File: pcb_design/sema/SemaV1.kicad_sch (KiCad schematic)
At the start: 22 parts, among them IC1 PIC24FJ64GA002-I_SP, J1 Conn_01x05_Pin, J2 Conn_01x02_Pin, J3 Conn_01x02_Pin, J4 Conn_01x04_Pin, U1 ESP8266-01_ESP-01

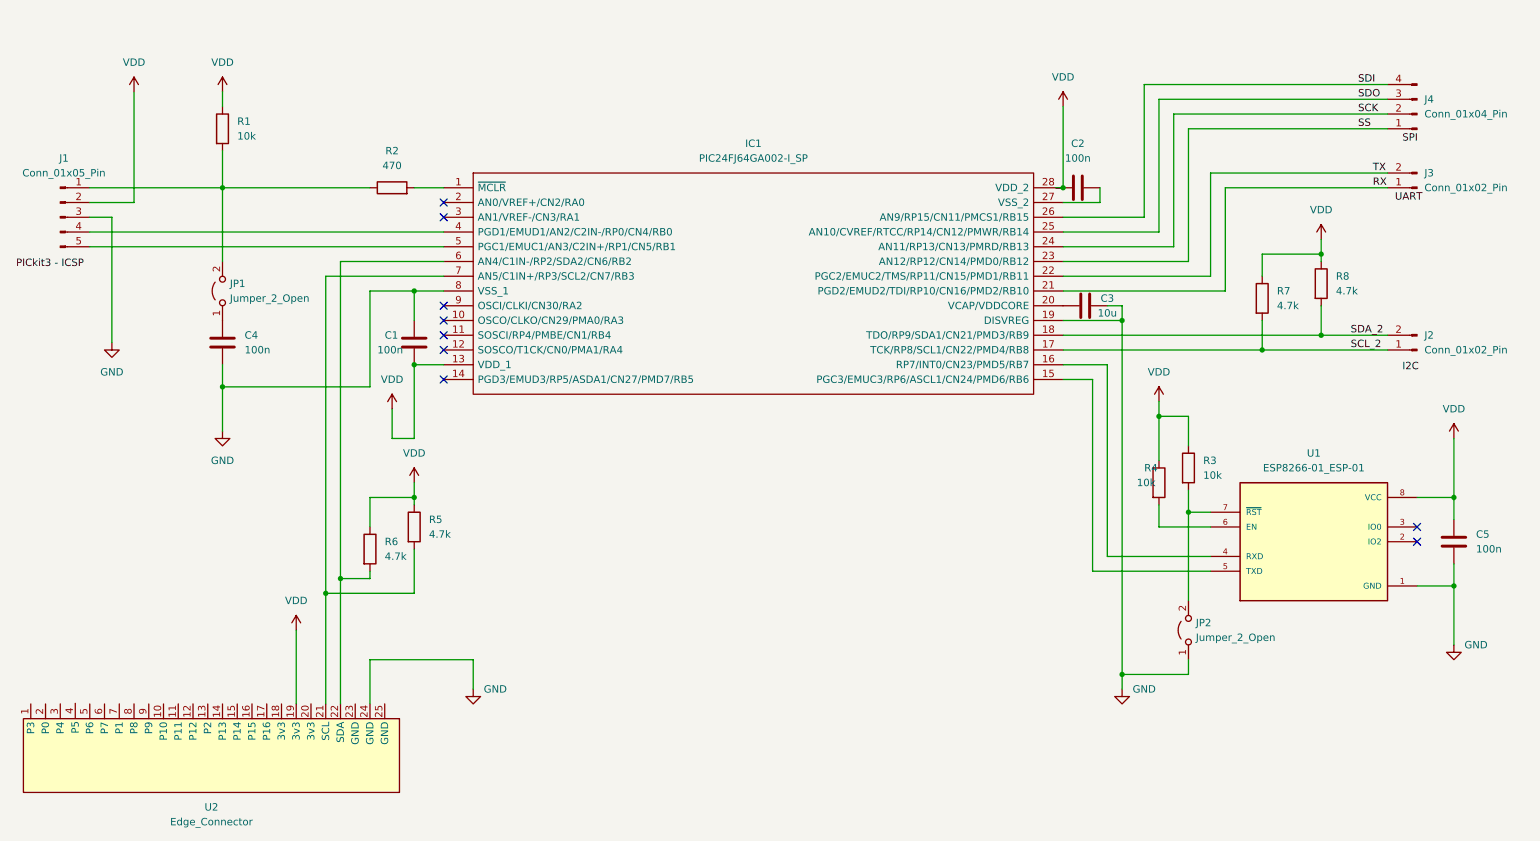
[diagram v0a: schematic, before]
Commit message: -Dodavanje testnih tacaka na semu, za potrebe kasnijeg testiranja
- Izmjena imena foldera iz semav1 u sema
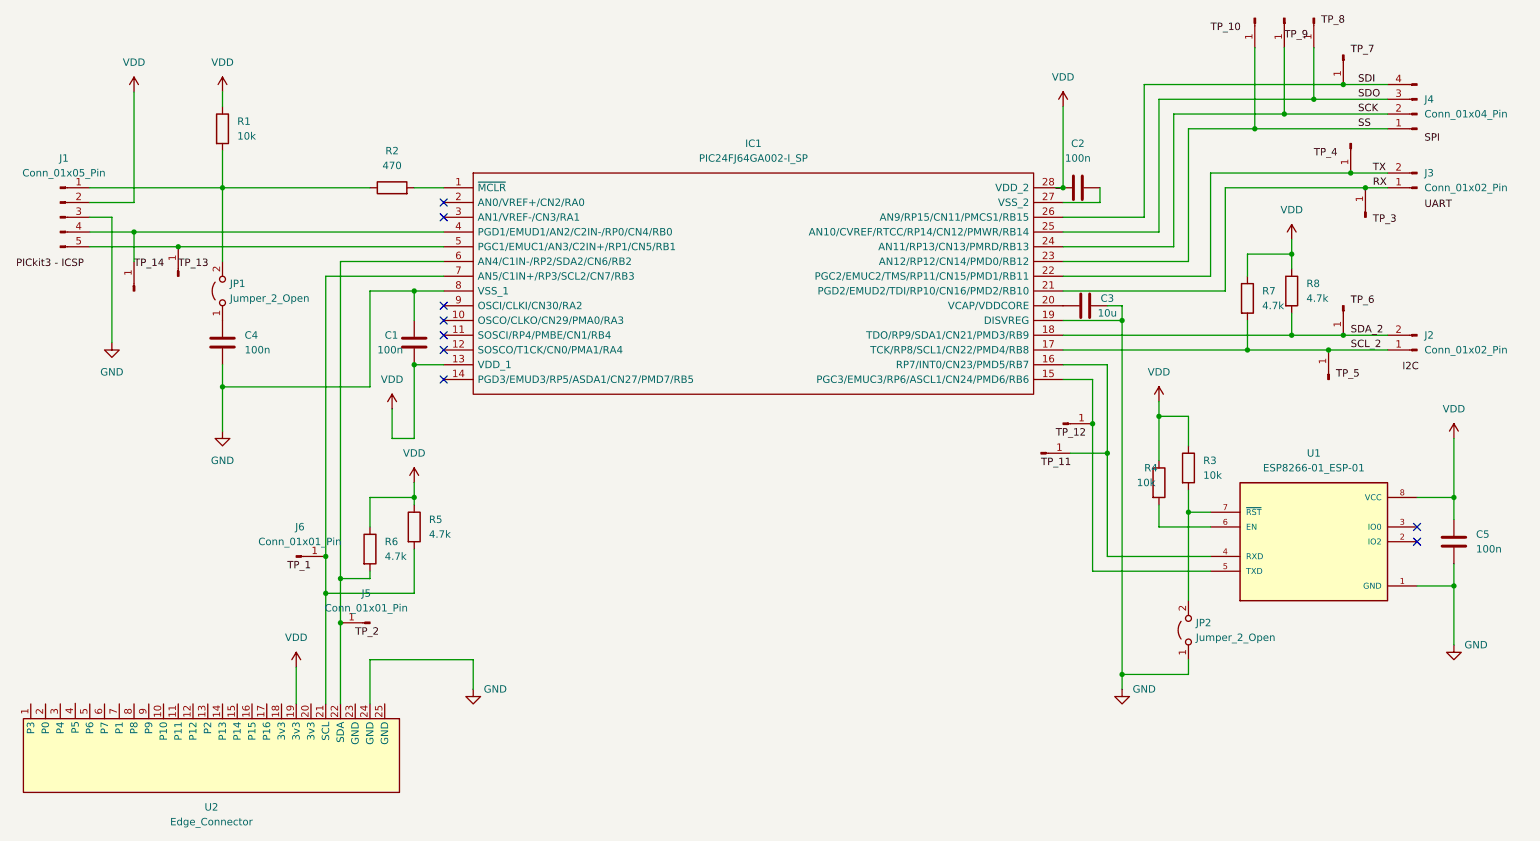
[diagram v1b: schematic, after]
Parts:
- added J10, J11, J12, J13, J14, J15, J16, J17, J18, J5, J6, J7, J8, J9: Conn_01x01_Pin, symbol Connector:Conn_01x01_Pin
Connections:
- net RX: now also J7.1 (Pin_1)
- net SCK: now also J13.1 (Pin_1)
- net SCL_2: now also J10.1 (Pin_1)
- net SDA_2: now also J9.1 (Pin_1)
- net SDI: now also J11.1 (Pin_1)
- net SDO: now also J12.1 (Pin_1)
- net SS: now also J14.1 (Pin_1)
- net TX: now also J8.1 (Pin_1)
- net at IC1.4 (PGD1/EMUD1/AN2/C2IN-/RP0/CN4/RB0), J1.4 (Pin_4): now also J17.1 (Pin_1)
- net at IC1.5 (PGC1/EMUC1/AN3/C2IN+/RP1/CN5/RB1), J1.5 (Pin_5): now also J18.1 (Pin_1)
- net at IC1.7 (AN5/C1IN+/RP3/SCL2/CN7/RB3), R5.2, U2.21 (SCL): now also J6.1 (Pin_1)
- net at IC1.6 (AN4/C1IN-/RP2/SDA2/CN6/RB2), R6.2, U2.22 (SDA): now also J5.1 (Pin_1)
- net at IC1.15 (PGC3/EMUC3/RP6/ASCL1/CN24/PMD6/RB6), U1.5 (TXD): now also J15.1 (Pin_1)
- net at IC1.16 (RP7/INT0/CN23/PMD5/RB7), U1.4 (RXD): now also J16.1 (Pin_1)
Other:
- moved on the sheet: R7, R8

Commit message: Dodavanje završnog dizajna pločice
Rutiranje komponenata
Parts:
- removed J10, J11, J12, J13, J14, J17, J18, J7, J8, J9: Conn_01x01_Pin, symbol Connector:Conn_01x01_Pin
- removed JP1, JP2: Jumper_2_Open, symbol Jumper:Jumper_2_Open
- removed U1: ESP8266-01_ESP-01, ESP8266-01_ESP-01:XCVR_ESP8266-01_ESP-01, symbol ESP8266-01_ESP-01:ESP8266-01_ESP-01
- added J19, J20: Conn_01x02_Pin, P_2_HEADER:HDRV2W66P0X254_1X2_508X254X874P, symbol Connector:Conn_01x02_Pin
- added U1: ESP8266-01_ESP-01, WiFi:XCVR_ESP8266-01_ESP-01, symbol WiFi:ESP8266-01_ESP-01
- C1, C2, C4, C5: footprint (none) -> CAP_0.1u:CAPC5750X270N
- C3: footprint (none) -> CAP_10u:C2220_FT
- I2C1: renamed from J2; footprint (none) -> P_2_HEADER:HDRV2W66P0X254_1X2_508X254X874P
- IC1: footprint KiCad:DIP794W56P254L3486H508Q28N -> PIC24FJ64GA002:DIP794W56P254L3486H508Q28N
- J1: footprint (none) -> P_5_HEADER:HDRV5W67P0X254_1X5_1229X234X821P
- J15, J16: footprint (none) -> Connector_Wire:SolderWire-0.1sqmm_1x01_D0.4mm_OD1mm
- R1, R3, R4: footprint (none) -> RES_10k:RESC6432X120N
- R2: footprint (none) -> RES_470:RESC6332X65N
- R5, R6, R7, R8: footprint (none) -> RES_4k7:RESC6432X65N
- SPI1: renamed from J4; footprint (none) -> P_4_HEADER:HDRV4W64P0X254_1X4_1016X254X889P
- TP_1: renamed from J6; footprint (none) -> Connector_Wire:SolderWire-0.1sqmm_1x01_D0.4mm_OD1mm
- TP_2: renamed from J5; footprint (none) -> Connector_Wire:SolderWire-0.1sqmm_1x01_D0.4mm_OD1mm
- U2: footprint (none) -> Edge_Connector_Library:Edge_Connector
- UART1: renamed from J3; footprint (none) -> P_2_HEADER:HDRV2W66P0X254_1X2_508X254X874P
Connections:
- net GND: now also J20.1 (Pin_1), U1.1 (GND)
- net VDD: now also U1.8 (VCC)
- net at R4.2: now also U1.6 (EN)
- net at J1.1 (Pin_1), R1.2, R2.1: now also J19.2 (Pin_2)
- net at R3.2: now also J20.2 (Pin_2), U1.7 (~{RST})
- net at IC1.15 (PGC3/EMUC3/RP6/ASCL1/CN24/PMD6/RB6), J15.1 (Pin_1): now also U1.5 (TXD)
- net at IC1.16 (RP7/INT0/CN23/PMD5/RB7), J16.1 (Pin_1): now also U1.4 (RXD)
- net at C4.1: now also J19.1 (Pin_1)
- no-connect marks 9 -> 30
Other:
- note added: "PICkit3 - ICSP"
- note added: "TP_11"
- note added: "TP_12"
- company: (none) -> ETF Banja Luka
- title: (none) -> AUTONOMNO VOZILO

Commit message: Dodavanje pcb fajla sa rutiranim komponentama
Sitne izmjene sa semi
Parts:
- removed U2: ~, Edge_Connector_Library:Edge_Connector, symbol Edge_Connector:Edge_Connector
- added U1: ~, Edge_Connector_Library:Edge_Connector, symbol Edge_Connector:Edge_Connector
- C1, C2, C4, C5: footprint CAP_0.1u:CAPC5750X270N -> CAP_0.1uF:C1812
- C3: footprint CAP_10u:C2220_FT -> CAP_10uF:C1812
- J1: value Conn_01x05_Pin -> PICkit3 - ICSP
- renumbered J20 to RST1, J16 to TP_RXD_WiFi1, TP_1 to TP_SCL1, TP_2 to TP_SDA1, J15 to TP_TXD_WiFI1, U1 to WiFi1
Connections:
- net GND: now also U1.24 (GND)
- net VDD: now also U1.19 (3v3)
- net at IC1.7 (AN5/C1IN+/RP3/SCL2/CN7/RB3), R5.2, TP_SCL1.1 (Pin_1): now also U1.21 (SCL)
- net at IC1.6 (AN4/C1IN-/RP2/SDA2/CN6/RB2), R6.2, TP_SDA1.1 (Pin_1): now also U1.22 (SDA)
- net SCL_2 renamed SCL_1
- net SDA_2 renamed SDA_1
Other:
- note removed: "PICkit3 - ICSP"
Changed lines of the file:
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@@
     (effects (font (size 1.27 1.27)) (justify left bottom))
   )
-  (text "PICkit3 - ICSP" (at 20.32 63.5 0)
-    (effects (font (size 1.27 1.27)) (justify left bottom))
-  )
-  (label "SCL_2" (at 250.19 77.47 0) (fields_autoplaced)
+  (label "SCL_1" (at 250.19 77.47 0) (fields_autoplaced)
     (effects (font (size 1.27 1.27)) (justify left bottom))
   )
@@
     (effects (font (size 1.27 1.27)) (justify left bottom))
   )
-  (label "SDA_2" (at 250.19 74.93 0) (fields_autoplaced)
+  (label "SDA_1" (at 250.19 74.93 0) (fields_autoplaced)
     (effects (font (size 1.27 1.27)) (justify left bottom))
   )
@@
     )
   )
+  (symbol (lib_id "Edge_Connector:Edge_Connector") (at 21.59 140.97 270) (unit 1)
+    (in_bom yes) (on_board yes) (dnp no) (fields_autoplaced)
+    (property "Reference" "U1" (at 53.975 156.21 90)
+      (effects (font (size 1.27 1.27)))
+    )
+    (property "Value" "~" (at 21.59 140.97 0)
+      (effects (font (size 1.27 1.27)))
+    )
+    (property "Footprint" "Edge_Connector_Library:Edge_Connector" (at 21.59 140.97 0)
+      (effects (font (size 1.27 1.27)) hide)
+    )
+    (property "Datasheet" "" (at 21.59 140.97 0)
+      (effects (font (size 1.27 1.27)) hide)
+    )
+    (property "Symbol Name" "Edge_Connector" (at 53.975 158.75 90)
+      (effects (font (size 1.27 1.27)))
+    )
+    (pin "11")
+    (pin "6")
+    (pin "22")
+    (pin "2")
+    (pin "19")
+    (pin "20")
+    (pin "25")
+    (pin "5")
+    (pin "23")
+    (pin "13")
+    (pin "7")
+    (pin "15")
+    (pin "10")
+    (pin "21")
+    (pin "24")
+    (pin "12")
+    (pin "1")
+    (pin "4")
+    (pin "18")
+    (pin "8")
+    (pin "14")
+    (pin "17")
+    (pin "16")
+    (pin "3")
+    (pin "9")
+    (instances
+      (project "SemaV1"
+        (path "/207b448c-7d7b-483b-97a4-67e5cc54f970"
+          (reference "U1") (unit 1)
+        )
+      )
+    )
+  )
   (symbol (lib_id "Connector:Conn_01x05_Pin") (at 27.94 54.61 0) (unit 1)
     (in_bom yes) (on_board yes) (dnp no) (fields_autoplaced)
@@
       (effects (font (size 1.27 1.27)))
     )
-    (property "Value" "Conn_01x05_Pin" (at 28.575 46.99 0)
+    (property "Value" "PICkit3 - ICSP" (at 28.575 46.99 0)
       (effects (font (size 1.27 1.27)))
     )
@@
   (symbol (lib_id "WiFi:ESP8266-01_ESP-01") (at 243.84 110.49 0) (unit 1)
     (in_bom yes) (on_board yes) (dnp no) (fields_autoplaced)
-    (property "Reference" "U1" (at 243.84 95.25 0)
+    (property "Reference" "WiFi1" (at 243.84 95.25 0)
       (effects (font (size 1.27 1.27)))
     )
@@
       (project "SemaV1"
         (path "/207b448c-7d7b-483b-97a4-67e5cc54f970"
-          (reference "U1") (unit 1)
+          (reference "WiFi1") (unit 1)
         )
       )
@@
   (symbol (lib_id "Connector:Conn_01x02_Pin") (at 227.33 127 180) (unit 1)
     (in_bom yes) (on_board yes) (dnp no) (fields_autoplaced)
-    (property "Reference" "J20" (at 228.6 124.46 0)
+    (property "Reference" "RST1" (at 228.6 124.46 0)
       (effects (font (size 1.27 1.27)) (justify right))
     )
@@
       (project "SemaV1"
         (path "/207b448c-7d7b-483b-97a4-67e5cc54f970"
-          (reference "J20") (unit 1)
+          (reference "RST1") (unit 1)
         )
       )
@@
   (symbol (lib_id "Connector:Conn_01x01_Pin") (at 68.58 113.03 0) (unit 1)
     (in_bom yes) (on_board yes) (dnp no) (fields_autoplaced)
-    (property "Reference" "TP_1" (at 69.215 107.95 0)
+    (property "Reference" "TP_SCL1" (at 69.215 107.95 0)
       (effects (font (size 1.27 1.27)))
     )
@@
       (project "SemaV1"
         (path "/207b448c-7d7b-483b-97a4-67e5cc54f970"
-          (reference "TP_1") (unit 1)
+          (reference "TP_SCL1") (unit 1)
         )
       )
@@
       (effects (font (size 1.27 1.27)))
     )
-    (property "Footprint" "CAP_0.1u:CAPC5750X270N" (at 207.01 48.5648 0)
+    (property "Footprint" "CAP_0.1uF:C1812" (at 207.01 48.5648 0)
       (effects (font (size 1.27 1.27)) hide)
     )
@@
       (effects (font (size 1.27 1.27)) (justify right))
     )
-    (property "Footprint" "CAP_0.1u:CAPC5750X270N" (at 267.0048 106.68 0)
+    (property "Footprint" "CAP_0.1uF:C1812" (at 267.0048 106.68 0)
       (effects (font (size 1.27 1.27)) hide)
     )
@@
       (effects (font (size 1.27 1.27)))
     )
-    (property "Footprint" "CAP_10u:C2220_FT" (at 208.28 68.8848 0)
+    (property "Footprint" "CAP_10uF:C1812" (at 208.28 68.8848 0)
       (effects (font (size 1.27 1.27)) hide)
     )
@@
         (path "/207b448c-7d7b-483b-97a4-67e5cc54f970"
           (reference "C3") (unit 1)
-        )
-      )
-    )
-  )
-  (symbol (lib_id "Edge_Connector:Edge_Connector") (at 21.59 140.97 270) (unit 1)
-    (in_bom yes) (on_board yes) (dnp no) (fields_autoplaced)
-    (property "Reference" "U2" (at 53.975 156.21 90)
-      (effects (font (size 1.27 1.27)))
-    )
-    (property "Value" "~" (at 21.59 140.97 0)
-      (effects (font (size 1.27 1.27)))
-    )
-    (property "Footprint" "Edge_Connector_Library:Edge_Connector" (at 21.59 140.97 0)
-      (effects (font (size 1.27 1.27)) hide)
-    )
-    (property "Datasheet" "" (at 21.59 140.97 0)
-      (effects (font (size 1.27 1.27)) hide)
-    )
-    (property "Symbol Name" "Edge_Connector" (at 53.975 158.75 90)
-      (effects (font (size 1.27 1.27)))
-    )
-    (pin "1")
-    (pin "10")
-    (pin "22")
-    (pin "8")
-    (pin "21")
-    (pin "12")
-    (pin "23")
-    (pin "25")
-    (pin "3")
-    (pin "20")
-    (pin "4")
-    (pin "7")
-    (pin "5")
-    (pin "2")
-    (pin "9")
-    (pin "15")
-    (pin "16")
-    (pin "18")
-    (pin "11")
-    (pin "14")
-    (pin "17")
-    (pin "19")
-    (pin "24")
-    (pin "6")
-    (pin "13")
-    (instances
-      (project "SemaV1"
-        (path "/207b448c-7d7b-483b-97a4-67e5cc54f970"
-          (reference "U2") (unit 1)
         )
       )
@@
       (effects (font (size 1.27 1.27)) (justify left))
     )
-    (property "Footprint" "CAP_0.1u:CAPC5750X270N" (at 89.8652 80.01 0)
+    (property "Footprint" "CAP_0.1uF:C1812" (at 89.8652 80.01 0)
       (effects (font (size 1.27 1.27)) hide)
     )
@@
   )
   (symbol (lib_id "Connector:Conn_01x01_Pin") (at 200.66 90.17 0) (unit 1)
-    (in_bom yes) (on_board yes) (dnp no) (fields_autoplaced)
-    (property "Reference" "J15" (at 201.295 85.09 0)
-      (effects (font (size 1.27 1.27)) hide)
+    (in_bom yes) (on_board yes) (dnp no)
+    (property "Reference" "TP_TXD_WiFI1" (at 200.66 86.36 0)
+      (effects (font (size 1.27 1.27)))
     )
     (property "Value" "Conn_01x01_Pin" (at 201.295 87.63 0)
@@
       (project "SemaV1"
         (path "/207b448c-7d7b-483b-97a4-67e5cc54f970"
-          (reference "J15") (unit 1)
+          (reference "TP_TXD_WiFI1") (unit 1)
         )
       )
@@
       (effects (font (size 1.27 1.27)) (justify left))
     )
-    (property "Footprint" "CAP_0.1u:CAPC5750X270N" (at 56.8452 80.01 0)
+    (property "Footprint" "CAP_0.1uF:C1812" (at 56.8452 80.01 0)
       (effects (font (size 1.27 1.27)) hide)
     )
@@
   )
   (symbol (lib_id "Connector:Conn_01x01_Pin") (at 196.85 95.25 0) (unit 1)
-    (in_bom yes) (on_board yes) (dnp no) (fields_autoplaced)
-    (property "Reference" "J16" (at 197.485 90.17 0)
-      (effects (font (size 1.27 1.27)) hide)
+    (in_bom yes) (on_board yes) (dnp no)
+    (property "Reference" "TP_RXD_WiFi1" (at 196.85 97.79 0)
+      (effects (font (size 1.27 1.27)))
     )
     (property "Value" "Conn_01x01_Pin" (at 197.485 92.71 0)
@@
       (project "SemaV1"
         (path "/207b448c-7d7b-483b-97a4-67e5cc54f970"
-          (reference "J16") (unit 1)
+          (reference "TP_RXD_WiFi1") (unit 1)
         )
       )
@@
   (symbol (lib_id "Connector:Conn_01x01_Pin") (at 81.28 124.46 180) (unit 1)
     (in_bom yes) (on_board yes) (dnp no)
-    (property "Reference" "TP_2" (at 83.82 124.46 0)
+    (property "Reference" "TP_SDA1" (at 83.82 124.46 0)
       (effects (font (size 1.27 1.27)))
     )
@@
       (project "SemaV1"
         (path "/207b448c-7d7b-483b-97a4-67e5cc54f970"
-          (reference "TP_2") (unit 1)
-        )
-      )
+          (reference "TP_SDA1") (unit 1)
+        )
+      )
